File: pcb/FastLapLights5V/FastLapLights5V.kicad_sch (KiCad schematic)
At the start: 29 parts, among them IC1 74HCT1G125GV,125, J1 POWER_CON, J2 SWD, J3 I2C, J4 IO, U1 STM32C011F4Px, U2 AP63205WU, U3 AP2112K-3.3, U4 BD33FC0FP

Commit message: change jlcpcb parts
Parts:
- removed C12: 0.1uF, Capacitor_SMD:C_0805_2012Metric, symbol Device:C_Small
- removed C13: 22uF, Capacitor_SMD:C_0603_1608Metric, symbol Device:C_Small
- removed C7, C8: 4.7uF, Capacitor_SMD:C_0603_1608Metric, symbol Device:C_Small
- removed U4: BD33FC0FP, Package_TO_SOT_SMD:TO-252-2, symbol Regulator_Linear:BD33FC0FP
- added C10, C11: 4.7uF, Capacitor_SMD:C_0603_1608Metric, symbol Device:C_Small
- C3: value 100uF -> 220uF; footprint Library:CP_Elec_A768KS227M1VLAE024 -> Library:CP_220_Honor_Elec_HV1E227M0810PZ; LCSC C3274444 -> C5246542
- C5: value 100nF -> 0.1uF; footprint Capacitor_SMD:C_0805_2012Metric -> Capacitor_SMD:C_0603_1608Metric; LCSC C519981 -> C1591
- C6: footprint Capacitor_SMD:C_0805_2012Metric -> Capacitor_SMD:C_0603_1608Metric; LCSC C519981 -> C1591
- C7: renamed from C9; footprint Capacitor_SMD:C_0805_2012Metric -> Capacitor_SMD:C_0603_1608Metric; LCSC C519981 -> C1591
- L1: value 22.8uH -> 22uH; footprint Library:L_EATON_DR1030-220-R -> Library:L_Chilisin_Elec_BPSC00101140220M00; LCSC C2638823 -> C5201662
- renumbered C14 to C12, C10 to C8, C11 to C9
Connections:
- net +3.3V: now also C11.1
- net +5V: now also C10.1
- net GND: now also C10.2, C11.2
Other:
- note added: "5V Supply"
- note removed: "Buck Converter (BC)"
- note removed: "LDO"
- note removed: "Optional 5V supply. Choose BC for start lights. Otherwise LDO is sufficient."
- moved on the sheet: C3, C4, C5, C6, C7, C8, C9, D1, L1, U2

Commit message: change sj start light - pit lane light
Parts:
- removed R1: 4k7, Resistor_SMD:R_0603_1608Metric, symbol Device:R_Small
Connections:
- net GND: now also JP1.1 (A)
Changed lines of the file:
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@@
 	(wire
 		(pts
+			(xy 168.91 57.15) (xy 168.91 58.42)
+		)
+		(stroke
+			(width 0)
+			(type default)
+		)
+	)
+	(wire
+		(pts
 			(xy 96.52 72.39) (xy 96.52 74.93)
 		)
@@
 	(wire
 		(pts
-			(xy 165.1 54.61) (xy 165.1 57.15)
+			(xy 168.91 57.15) (xy 170.18 57.15)
 		)
 		(stroke
@@
 	(wire
 		(pts
-			(xy 165.1 57.15) (xy 170.18 57.15)
-		)
-		(stroke
-			(width 0)
-			(type default)
-		)
-	)
-	(wire
-		(pts
 			(xy 132.08 168.91) (xy 132.08 171.45)
 		)
@@
 	(wire
 		(pts
-			(xy 165.1 48.26) (xy 165.1 49.53)
-		)
-		(stroke
-			(width 0)
-			(type default)
-		)
-	)
-	(wire
-		(pts
 			(xy 78.74 171.45) (xy 83.82 171.45)
 		)
@@
 	(symbol
 		(lib_id "power:GND")
+		(at 168.91 58.42 0)
+		(unit 1)
+		(exclude_from_sim no)
+		(in_bom yes)
+		(on_board yes)
+		(dnp no)
+		(fields_autoplaced yes)
+		(property "Reference" "#PWR7"
+			(at 168.91 64.77 0)
+			(effects
+				(font
+					(size 1.27 1.27)
+				)
+				(hide yes)
+			)
+		)
+		(property "Value" "GND"
+			(at 168.91 63.5 0)
+			(effects
+				(font
+					(size 1.27 1.27)
+				)
+			)
+		)
+		(property "Footprint" ""
+			(at 168.91 58.42 0)
+			(effects
+				(font
+					(size 1.27 1.27)
+				)
+				(hide yes)
+			)
+		)
+		(property "Datasheet" ""
+			(at 168.91 58.42 0)
+			(effects
+				(font
+					(size 1.27 1.27)
+				)
+				(hide yes)
+			)
+		)
+		(property "Description" "Power symbol creates a global label with name \"GND\" , ground"
+			(at 168.91 58.42 0)
+			(effects
+				(font
+					(size 1.27 1.27)
+				)
+				(hide yes)
+			)
+		)
+		(pin "1"
+		)
+		(instances
+			(project ""
+				(path "/b6918c10-7d8e-4015-89e0-e42eef76cd26"
+					(reference "#PWR7")
+					(unit 1)
+				)
+			)
+		)
+	)
+	(symbol
+		(lib_id "power:GND")
 		(at 234.95 109.22 0)
 		(unit 1)
@@
 	)
 	(symbol
-		(lib_id "Device:R_Small")
-		(at 165.1 52.07 0)
-		(unit 1)
-		(exclude_from_sim no)
-		(in_bom yes)
-		(on_board yes)
-		(dnp no)
-		(property "Reference" "R1"
-			(at 166.878 50.8 0)
-			(effects
-				(font
-					(size 1.27 1.27)
-				)
-				(justify left)
-			)
-		)
-		(property "Value" "4k7"
-			(at 166.878 52.832 0)
-			(effects
-				(font
-					(size 1.27 1.27)
-				)
-				(justify left)
-			)
-		)
-		(property "Footprint" "Resistor_SMD:R_0603_1608Metric"
-			(at 165.1 52.07 0)
-			(effects
-				(font
-					(size 1.27 1.27)
-				)
-				(hide yes)
-			)
-		)
-		(property "Datasheet" "~"
-			(at 165.1 52.07 0)
-			(effects
-				(font
-					(size 1.27 1.27)
-				)
-				(hide yes)
-			)
-		)
-		(property "Description" "Resistor, small symbol"
-			(at 165.1 52.07 0)
-			(effects
-				(font
-					(size 1.27 1.27)
-				)
-				(hide yes)
-			)
-		)
-		(property "Field5" ""
-			(at 165.1 52.07 0)
-			(effects
-				(font
-					(size 1.27 1.27)
-				)
-				(hide yes)
-			)
-		)
-		(property "LCSC" "C99782"
-			(at 165.1 52.07 0)
-			(effects
-				(font
-					(size 1.27 1.27)
-				)
-				(hide yes)
-			)
-		)
-		(pin "1"
-		)
-		(pin "2"
-		)
-		(instances
-			(project "FastLapLights5V"
-				(path "/b6918c10-7d8e-4015-89e0-e42eef76cd26"
-					(reference "R1")
-					(unit 1)
-				)
-			)
-		)
-	)
-	(symbol
 		(lib_id "Device:C_Small")
 		(at 85.09 118.11 0)
@@
 					(unit 1)
 				)
-			)
-		)
-	)
-	(symbol
-		(lib_id "power:+3.3V")
-		(at 165.1 48.26 0)
-		(unit 1)
-		(exclude_from_sim no)
-		(in_bom yes)
-		(on_board yes)
-		(dnp no)
-		(fields_autoplaced yes)
-		(property "Reference" "#PWR7"
-			(at 165.1 52.07 0)
-			(effects
-				(font
-					(size 1.27 1.27)
-				)
-				(hide yes)
-			)
-		)
-		(property "Value" "+3.3V"
-			(at 165.1 43.18 0)
-			(effects
-				(font
-					(size 1.27 1.27)
-				)
-			)
-		)
-		(property "Footprint" ""
-			(at 165.1 48.26 0)
-			(effects
-				(font
-					(size 1.27 1.27)
-				)
-				(hide yes)
-			)
-		)
-		(property "Datasheet" ""
-			(at 165.1 48.26 0)
-			(effects
-				(font
-					(size 1.27 1.27)
-				)
-				(hide yes)
-			)
-		)
-		(property "Description" "Power symbol creates a global label with name \"+3.3V\""
-			(at 165.1 48.26 0)
-			(effects
-				(font
-					(size 1.27 1.27)
-				)
-				(hide yes)
-			)
-		)
-		(pin "1"
-		)
-		(instances
-			(project "FastLapLights5V"
-				(path "/b6918c10-7d8e-4015-89e0-e42eef76cd26"
-					(reference "#PWR7")
-					(unit 1)
-				)

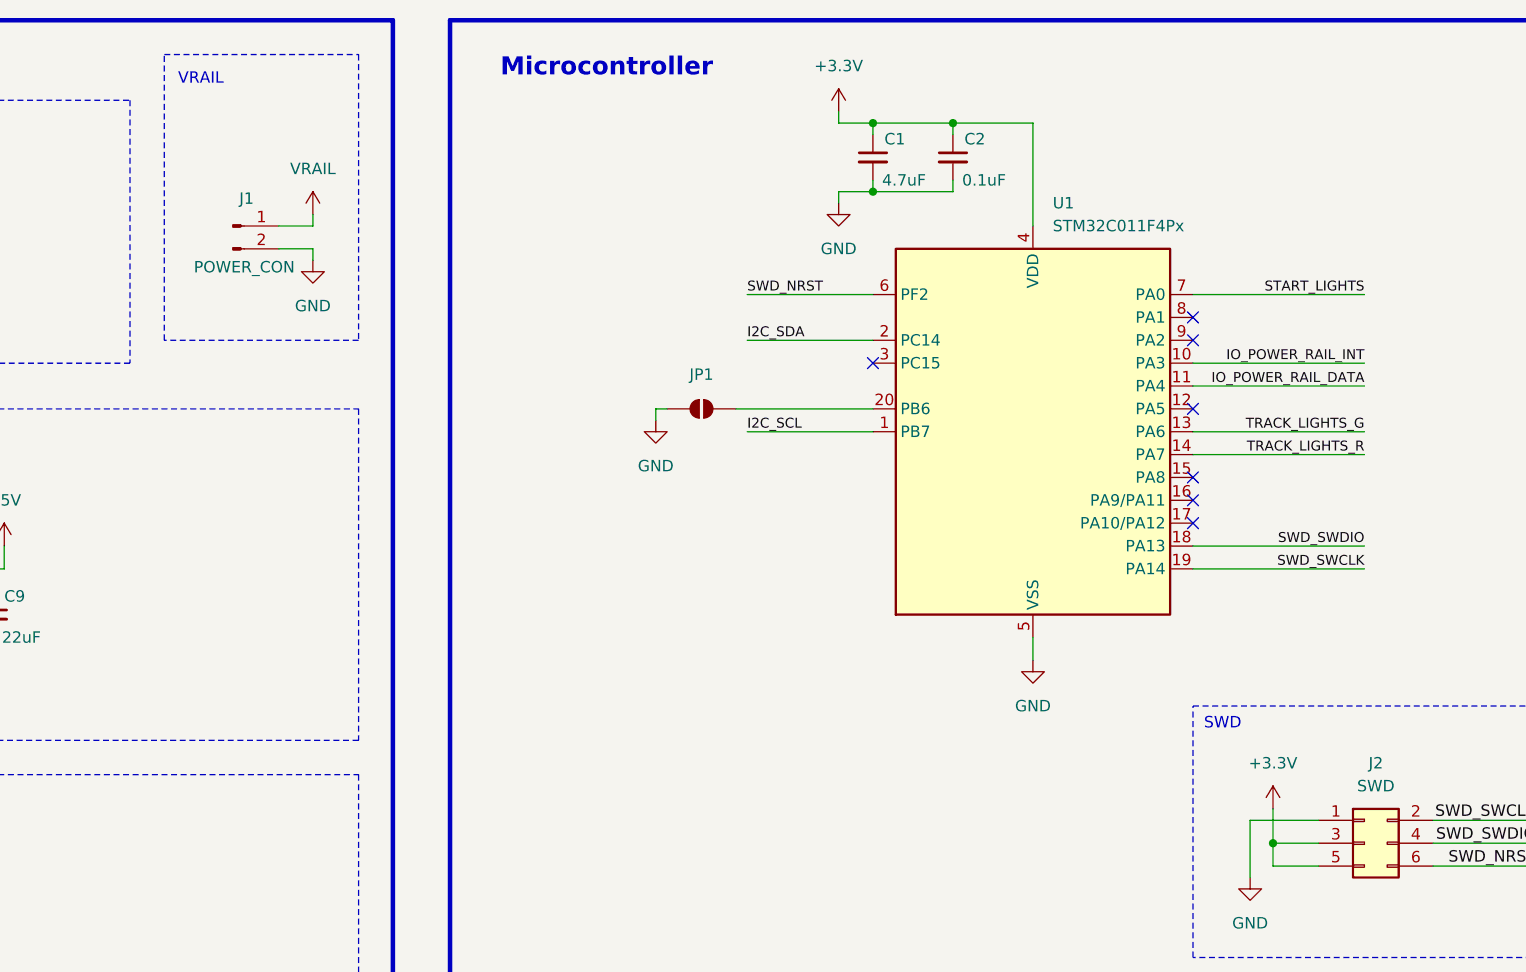
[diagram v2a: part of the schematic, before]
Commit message: fix issues with decoding manchester data and make it more reliable
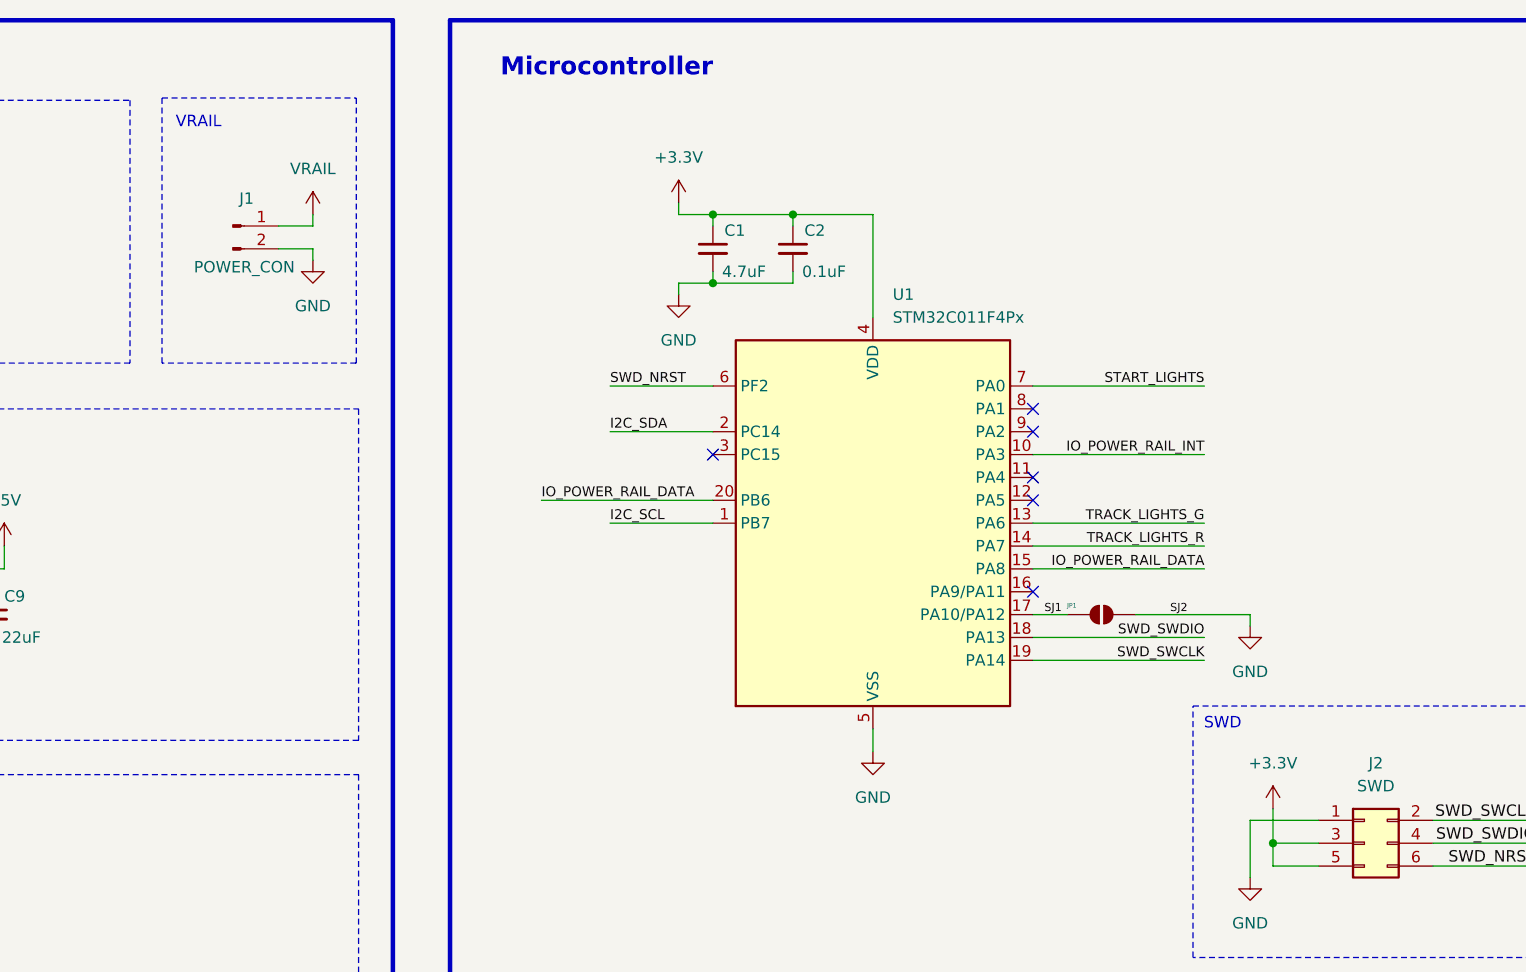
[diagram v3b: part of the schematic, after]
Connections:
- net GND: now also JP1.2 (B); no longer JP1.1 (A)
- net IO_POWER_RAIL_DATA: now also U1.15 (PA8), U1.20 (PB6); no longer U1.11 (PA4)
- net SJ1: now reaches U1.17 (PA10/PA12)
- net SJ1: now also JP1.1 (A)
- no-connect marks 7 -> 6
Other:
- moved on the sheet: C1, C2, JP1, U1

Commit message: activate solder jumper pin, replace sold-out components
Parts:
- L1: footprint Library:L_Chilisin_Elec_BPSC00101140220M00 -> Library:L_SXN_SMDRH104R-220MT; LCSC C5201662 -> C72414
- U3: LCSC C51118 -> C3021085
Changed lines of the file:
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@@
 			)
 		)
-		(property "Footprint" "Library:L_Chilisin_Elec_BPSC00101140220M00"
+		(property "Footprint" "Library:L_SXN_SMDRH104R-220MT"
 			(at 80.01 64.77 0)
 			(effects
@@
 			)
 		)
-		(property "Datasheet" "https://www.lcsc.com/datasheet/lcsc_datasheet_2410121503_Chilisin-Elec-BPSC00101140220M00_C5201662.pdf"
+		(property "Datasheet" ""
 			(at 80.01 64.77 0)
 			(effects
@@
 			)
 		)
-		(property "LCSC" "C5201662"
+		(property "LCSC" "C72414"
 			(at 80.01 64.77 90)
 			(effects
@@
 			)
 		)
-		(property "LCSC" "C51118"
+		(property "LCSC" " C3021085"
 			(at 74.93 115.57 0)
 			(effects
